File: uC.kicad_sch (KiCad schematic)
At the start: 31 parts, among them J1 Analog, J2 Digital, J3 CANBUS, J4 UART, J5 SPI, J6 I2C, U1 PIC32MX775F256L-80I{slash}PT, Y1 Crystal

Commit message: Fixed nINT not actually being connected to 3v3 Changed the pic32MX7* 100 pin footprint from the T package to the F package Added some silkscreen around the DIGITAL and ANALOG headers
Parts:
- U1: footprint ul_PIC32MX775F256L-80I-PT:PIC32MX775F256L-80I&slash_PT -> ul_PIC32MX764F128L-I-PF:PIC32MX764F128L-I&slash_PF
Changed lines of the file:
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@@
       (effects (font (size 1.524 1.524)))
     )
-    (property "Footprint" "ul_PIC32MX775F256L-80I-PT:PIC32MX775F256L-80I&slash_PT" (id 2) (at 142.24 19.304 0)
+    (property "Footprint" "ul_PIC32MX764F128L-I-PF:PIC32MX764F128L-I&slash_PF" (id 2) (at 142.24 19.304 0)
       (effects (font (size 1.524 1.524)) hide)
     )

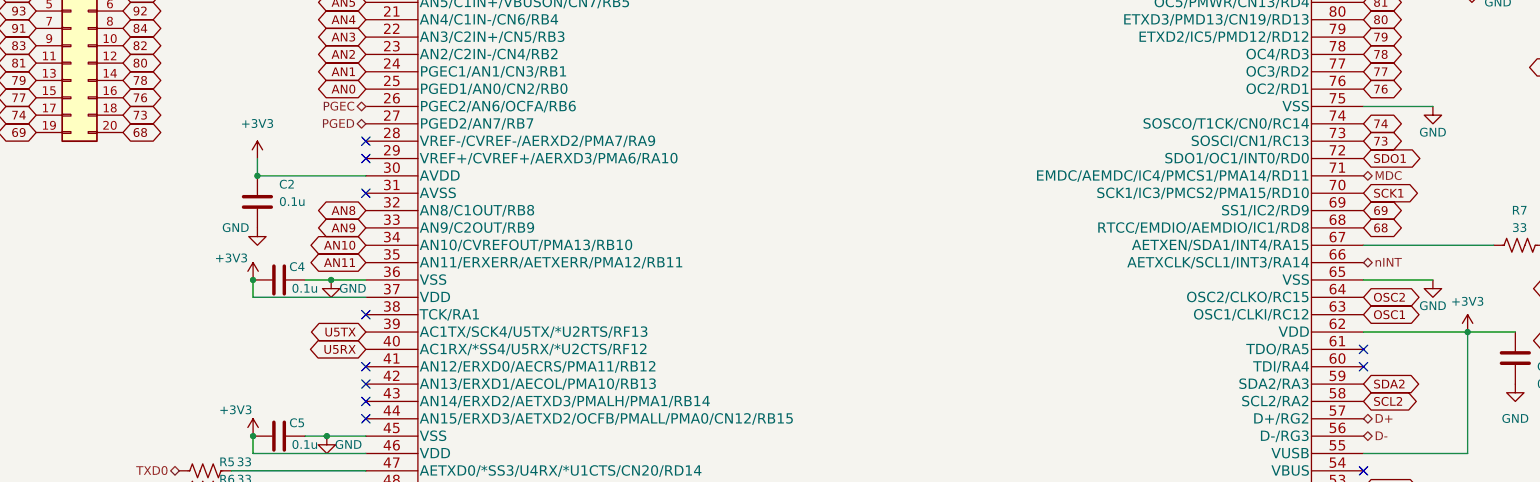
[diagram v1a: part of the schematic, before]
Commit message: Added connection for MDIO to the PIC Complete redesign of board, reduced size from 100x50 to 75x35mm Readded C15 and C16 to the front Added some test points
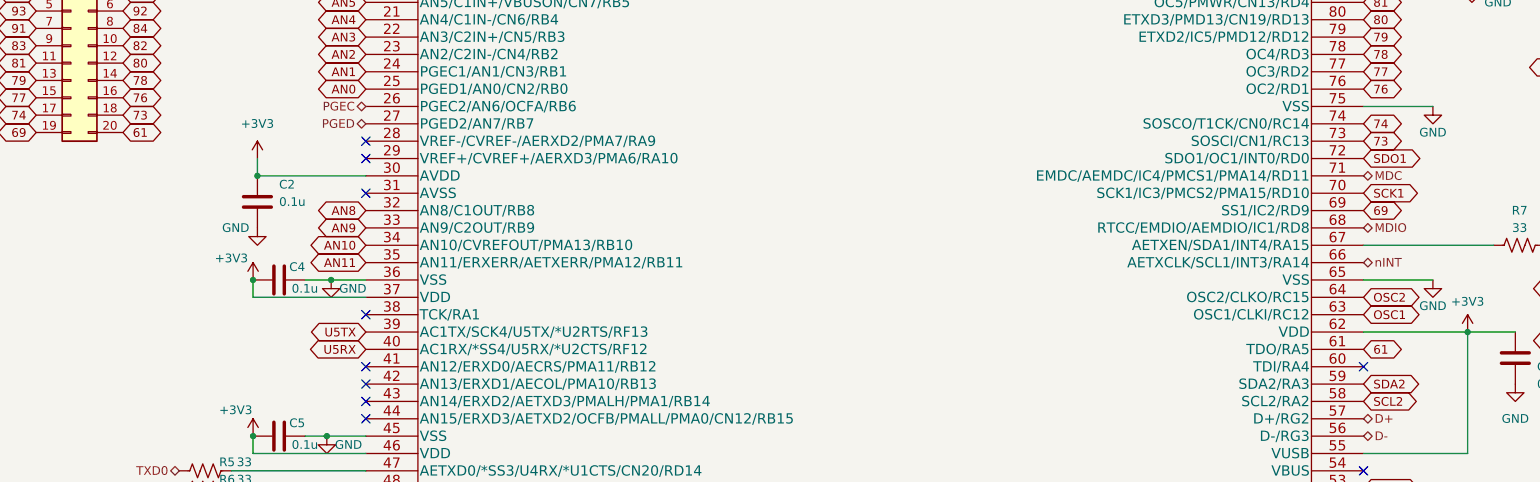
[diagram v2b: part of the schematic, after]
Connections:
- net 61: now reaches U1.61 (TDO/RA5)
- net 61: now also J2.20 (Pin_20)
- net 68 renamed MDIO
- net MDIO: no longer J2.20 (Pin_20)
- no-connect marks 21 -> 20
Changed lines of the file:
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@@
   (no_connect (at 218.44 142.24))
   (no_connect (at 218.44 149.86))
-  (no_connect (at 218.44 124.46))
   (no_connect (at 218.44 127))
   (no_connect (at 72.39 134.62))
@@
     )
   )
-  (global_label "68" (shape bidirectional) (at 218.44 106.68 0) (fields_autoplaced)
-    (effects (font (size 1.27 1.27)) (justify left))
-    (property "Intersheet References" "${INTERSHEET_REFS}" (id 0) (at 223.2721 106.6006 0)
-      (effects (font (size 1.27 1.27)) (justify left) hide)
-    )
-  )
   (global_label "91" (shape bidirectional) (at 218.44 48.26 0) (fields_autoplaced)
     (effects (font (size 1.27 1.27)) (justify left))
@@
     )
   )
+  (global_label "61" (shape bidirectional) (at 218.44 124.46 0) (fields_autoplaced)
+    (effects (font (size 1.27 1.27)) (justify left))
+    (property "Intersheet References" "${INTERSHEET_REFS}" (id 0) (at 223.2721 124.3806 0)
+      (effects (font (size 1.27 1.27)) (justify left) hide)
+    )
+  )
   (global_label "79" (shape bidirectional) (at 24.13 85.09 180) (fields_autoplaced)
     (effects (font (size 1.27 1.27)) (justify right))
@@
     )
   )
-  (global_label "68" (shape bidirectional) (at 36.83 92.71 0) (fields_autoplaced)
+  (global_label "AN3" (shape bidirectional) (at 72.39 78.74 180) (fields_autoplaced)
+    (effects (font (size 1.27 1.27)) (justify right))
+    (property "Intersheet References" "${INTERSHEET_REFS}" (id 0) (at 66.3483 78.6606 0)
+      (effects (font (size 1.27 1.27)) (justify right) hide)
+    )
+  )
+  (global_label "U2TX" (shape bidirectional) (at 252.095 43.18 180) (fields_autoplaced)
+    (effects (font (size 1.27 1.27)) (justify right))
+    (property "Intersheet References" "${INTERSHEET_REFS}" (id 0) (at 244.9648 43.2594 0)
+      (effects (font (size 1.27 1.27)) (justify right) hide)
+    )
+  )
+  (global_label "AN8" (shape bidirectional) (at 72.39 104.14 180) (fields_autoplaced)
+    (effects (font (size 1.27 1.27)) (justify right))
+    (property "Intersheet References" "${INTERSHEET_REFS}" (id 0) (at 66.3483 104.0606 0)
+      (effects (font (size 1.27 1.27)) (justify right) hide)
+    )
+  )
+  (global_label "LED3" (shape bidirectional) (at 31.75 185.42 180) (fields_autoplaced)
+    (effects (font (size 1.27 1.27)) (justify right))
+    (property "Intersheet References" "${INTERSHEET_REFS}" (id 0) (at 24.6802 185.3406 0)
+      (effects (font (size 1.27 1.27)) (justify right) hide)
+    )
+  )
+  (global_label "61" (shape bidirectional) (at 36.83 92.71 0) (fields_autoplaced)
     (effects (font (size 1.27 1.27)) (justify left))
     (property "Intersheet References" "${INTERSHEET_REFS}" (id 0) (at 41.6621 92.6306 0)
@@
     )
   )
-  (global_label "AN3" (shape bidirectional) (at 72.39 78.74 180) (fields_autoplaced)
-    (effects (font (size 1.27 1.27)) (justify right))
-    (property "Intersheet References" "${INTERSHEET_REFS}" (id 0) (at 66.3483 78.6606 0)
-      (effects (font (size 1.27 1.27)) (justify right) hide)
-    )
-  )
-  (global_label "U2TX" (shape bidirectional) (at 252.095 43.18 180) (fields_autoplaced)
-    (effects (font (size 1.27 1.27)) (justify right))
-    (property "Intersheet References" "${INTERSHEET_REFS}" (id 0) (at 244.9648 43.2594 0)
-      (effects (font (size 1.27 1.27)) (justify right) hide)
-    )
-  )
-  (global_label "AN8" (shape bidirectional) (at 72.39 104.14 180) (fields_autoplaced)
-    (effects (font (size 1.27 1.27)) (justify right))
-    (property "Intersheet References" "${INTERSHEET_REFS}" (id 0) (at 66.3483 104.0606 0)
-      (effects (font (size 1.27 1.27)) (justify right) hide)
-    )
-  )
-  (global_label "LED3" (shape bidirectional) (at 31.75 185.42 180) (fields_autoplaced)
-    (effects (font (size 1.27 1.27)) (justify right))
-    (property "Intersheet References" "${INTERSHEET_REFS}" (id 0) (at 24.6802 185.3406 0)
-      (effects (font (size 1.27 1.27)) (justify right) hide)
-    )
-  )
   (global_label "C2RX" (shape bidirectional) (at 218.44 50.8 0) (fields_autoplaced)
     (effects (font (size 1.27 1.27)) (justify left))
@@
     (effects (font (size 1.27 1.27)) (justify right))
   )
+  (hierarchical_label "MDIO" (shape bidirectional) (at 218.44 106.68 0)
+    (effects (font (size 1.27 1.27)) (justify left))
+  )
   (hierarchical_label "RX_ER" (shape bidirectional) (at 72.39 25.4 180)
